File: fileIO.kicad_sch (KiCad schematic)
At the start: 24 parts, among them J3 USB_C, J5 Conn_02x03_Odd_Even, SW1 SW_Push

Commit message: Fix some checker complaints
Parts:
- TP1, TP19, TP2, TP20, TP26, TP27, TP29, TP30, TP31, TP32: value (none) -> SMD_TP; footprint (none) -> gkl_misc:TestPoint_Pad_D0.5mm
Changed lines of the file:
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@@
       (effects (font (size 1.27 1.27)) (justify right))
     )
-    (property "Value" "" (id 1) (at 43.3324 140.8938 0)
-      (effects (font (size 1.27 1.27)) (justify right) hide)
-    )
-    (property "Footprint" "" (id 2) (at 49.53 140.97 0)
+    (property "Value" "SMD_TP" (id 1) (at 43.3324 140.8938 0)
+      (effects (font (size 1.27 1.27)) (justify right) hide)
+    )
+    (property "Footprint" "gkl_misc:TestPoint_Pad_D0.5mm" (id 2) (at 49.53 140.97 0)
       (effects (font (size 1.27 1.27)) hide)
     )
@@
       (effects (font (size 1.27 1.27)) (justify right))
     )
-    (property "Value" "" (id 1) (at 43.3324 143.4338 0)
-      (effects (font (size 1.27 1.27)) (justify right) hide)
-    )
-    (property "Footprint" "" (id 2) (at 49.53 143.51 0)
+    (property "Value" "SMD_TP" (id 1) (at 43.3324 143.4338 0)
+      (effects (font (size 1.27 1.27)) (justify right) hide)
+    )
+    (property "Footprint" "gkl_misc:TestPoint_Pad_D0.5mm" (id 2) (at 49.53 143.51 0)
       (effects (font (size 1.27 1.27)) hide)
     )
@@
       (effects (font (size 1.27 1.27)) (justify right))
     )
-    (property "Value" "" (id 1) (at 43.3324 159.9438 0)
-      (effects (font (size 1.27 1.27)) (justify right) hide)
-    )
-    (property "Footprint" "" (id 2) (at 49.53 160.02 0)
+    (property "Value" "SMD_TP" (id 1) (at 43.3324 159.9438 0)
+      (effects (font (size 1.27 1.27)) (justify right) hide)
+    )
+    (property "Footprint" "gkl_misc:TestPoint_Pad_D0.5mm" (id 2) (at 49.53 160.02 0)
       (effects (font (size 1.27 1.27)) hide)
     )
@@
       (effects (font (size 1.27 1.27)) (justify right))
     )
-    (property "Value" "" (id 1) (at 43.3324 162.4838 0)
-      (effects (font (size 1.27 1.27)) (justify right) hide)
-    )
-    (property "Footprint" "" (id 2) (at 49.53 162.56 0)
+    (property "Value" "SMD_TP" (id 1) (at 43.3324 162.4838 0)
+      (effects (font (size 1.27 1.27)) (justify right) hide)
+    )
+    (property "Footprint" "gkl_misc:TestPoint_Pad_D0.5mm" (id 2) (at 49.53 162.56 0)
       (effects (font (size 1.27 1.27)) hide)
     )
@@
       (effects (font (size 1.27 1.27)) (justify right))
     )
-    (property "Value" "" (id 1) (at 43.3324 157.4038 0)
-      (effects (font (size 1.27 1.27)) (justify right) hide)
-    )
-    (property "Footprint" "" (id 2) (at 49.53 157.48 0)
+    (property "Value" "SMD_TP" (id 1) (at 43.3324 157.4038 0)
+      (effects (font (size 1.27 1.27)) (justify right) hide)
+    )
+    (property "Footprint" "gkl_misc:TestPoint_Pad_D0.5mm" (id 2) (at 49.53 157.48 0)
       (effects (font (size 1.27 1.27)) hide)
     )
@@
       (effects (font (size 1.27 1.27)) (justify right))
     )
-    (property "Value" "" (id 1) (at 43.3324 154.8638 0)
-      (effects (font (size 1.27 1.27)) (justify right) hide)
-    )
-    (property "Footprint" "" (id 2) (at 49.53 154.94 0)
+    (property "Value" "SMD_TP" (id 1) (at 43.3324 154.8638 0)
+      (effects (font (size 1.27 1.27)) (justify right) hide)
+    )
+    (property "Footprint" "gkl_misc:TestPoint_Pad_D0.5mm" (id 2) (at 49.53 154.94 0)
       (effects (font (size 1.27 1.27)) hide)
     )
@@
       (effects (font (size 1.27 1.27)) (justify right))
     )
-    (property "Value" "" (id 1) (at 40.4876 172.6438 0)
-      (effects (font (size 1.27 1.27)) (justify right) hide)
-    )
-    (property "Footprint" "" (id 2) (at 34.29 172.72 0)
+    (property "Value" "SMD_TP" (id 1) (at 40.4876 172.6438 0)
+      (effects (font (size 1.27 1.27)) (justify right) hide)
+    )
+    (property "Footprint" "gkl_misc:TestPoint_Pad_D0.5mm" (id 2) (at 34.29 172.72 0)
       (effects (font (size 1.27 1.27)) hide)
     )
@@
       (effects (font (size 1.27 1.27)) (justify right))
     )
-    (property "Value" "" (id 1) (at 40.4876 175.1838 0)
-      (effects (font (size 1.27 1.27)) (justify right) hide)
-    )
-    (property "Footprint" "" (id 2) (at 34.29 175.26 0)
+    (property "Value" "SMD_TP" (id 1) (at 40.4876 175.1838 0)
+      (effects (font (size 1.27 1.27)) (justify right) hide)
+    )
+    (property "Footprint" "gkl_misc:TestPoint_Pad_D0.5mm" (id 2) (at 34.29 175.26 0)
       (effects (font (size 1.27 1.27)) hide)
     )
@@
       (effects (font (size 1.27 1.27)) (justify right))
     )
-    (property "Value" "" (id 1) (at 72.5424 140.8938 0)
-      (effects (font (size 1.27 1.27)) (justify right) hide)
-    )
-    (property "Footprint" "" (id 2) (at 78.74 140.97 0)
+    (property "Value" "SMD_TP" (id 1) (at 72.5424 140.8938 0)
+      (effects (font (size 1.27 1.27)) (justify right) hide)
+    )
+    (property "Footprint" "gkl_misc:TestPoint_Pad_D0.5mm" (id 2) (at 78.74 140.97 0)
       (effects (font (size 1.27 1.27)) hide)
     )
@@
       (effects (font (size 1.27 1.27)) (justify right))
     )
-    (property "Value" "" (id 1) (at 72.5424 143.4338 0)
-      (effects (font (size 1.27 1.27)) (justify right) hide)
-    )
-    (property "Footprint" "" (id 2) (at 78.74 143.51 0)
-      (effects (font (size 1.27 1.27)) hide)
-    )
+    (property "Value" "SMD_TP" (id 1) (at 72.5424 143.4338 0)
+      (effects (font (size 1.27 1.27)) (justify right) hide)
+    )
+    (property "Footprint" "gkl_misc:TestPoint_Pad_D0.5mm" (id 2) (at 78.74 143.51 0)
+      (effects (font (size 1.27 1.27)) hide)
+    )

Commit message: Update Mouser prices
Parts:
- C76: Pricing (EUR) 0,11 -> 0,09
- D1: Pricing (EUR) 1,85 -> 2,03
- J3: Pricing (EUR) 0,71 -> 0,77
- R21, R29, R4: Pricing (EUR) 0,11 -> 0,10
- R22, R23, R24, R32, R33: Pricing (EUR) 0,09 -> 0,10
- SW1: Pricing (EUR) 4,02 -> 5,11
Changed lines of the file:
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@@
       (effects (font (size 1.27 1.27)) hide)
     )
-    (property "Pricing (EUR)" "0,71" (id 7) (at 38.1 77.47 0)
+    (property "Pricing (EUR)" "0,77" (id 7) (at 38.1 77.47 0)
       (effects (font (size 1.27 1.27)) hide)
     )
@@
       (effects (font (size 1.27 1.27)) hide)
     )
-    (property "Pricing (EUR)" "0,09" (id 7) (at 214.63 29.21 0)
+    (property "Pricing (EUR)" "0,10" (id 7) (at 214.63 29.21 0)
       (effects (font (size 1.27 1.27)) hide)
     )
@@
       (effects (font (size 1.27 1.27)) hide)
     )
-    (property "Pricing (EUR)" "0,09" (id 7) (at 214.63 34.29 0)
+    (property "Pricing (EUR)" "0,10" (id 7) (at 214.63 34.29 0)
       (effects (font (size 1.27 1.27)) hide)
     )
@@
       (effects (font (size 1.27 1.27)) hide)
     )
-    (property "Pricing (EUR)" "4,02" (id 7) (at 133.35 44.45 0)
+    (property "Pricing (EUR)" "5,11" (id 7) (at 133.35 44.45 0)
       (effects (font (size 1.27 1.27)) hide)
     )
@@
       (effects (font (size 1.27 1.27)) hide)
     )
-    (property "Pricing (EUR)" "0,11" (id 7) (at 144.78 38.1 0)
+    (property "Pricing (EUR)" "0,10" (id 7) (at 144.78 38.1 0)
       (effects (font (size 1.27 1.27)) hide)
     )
@@
       (effects (font (size 1.27 1.27)) hide)
     )
-    (property "Pricing (EUR)" "0,11" (id 7) (at 148.59 49.53 0)
+    (property "Pricing (EUR)" "0,09" (id 7) (at 148.59 49.53 0)
       (effects (font (size 1.27 1.27)) hide)
     )
@@
       (effects (font (size 1.27 1.27)) hide)
     )
-    (property "Pricing (EUR)" "0,11" (id 7) (at 76.2 80.01 0)
+    (property "Pricing (EUR)" "0,10" (id 7) (at 76.2 80.01 0)
       (effects (font (size 1.27 1.27)) hide)
     )
@@
       (effects (font (size 1.27 1.27)) hide)
     )
-    (property "Pricing (EUR)" "0,11" (id 7) (at 76.2 77.47 0)
+    (property "Pricing (EUR)" "0,10" (id 7) (at 76.2 77.47 0)
       (effects (font (size 1.27 1.27)) hide)
     )
@@
       (effects (font (size 1.27 1.27)) hide)
     )
-    (property "Pricing (EUR)" "0,09" (id 7) (at 214.63 39.37 0)
+    (property "Pricing (EUR)" "0,10" (id 7) (at 214.63 39.37 0)
       (effects (font (size 1.27 1.27)) hide)
     )
@@
       (effects (font (size 1.27 1.27)) hide)
     )
-    (property "Pricing (EUR)" "1,85" (id 7) (at 226.06 34.29 0)
+    (property "Pricing (EUR)" "2,03" (id 7) (at 226.06 34.29 0)
       (effects (font (size 1.27 1.27)) hide)
     )
@@
       (effects (font (size 1.27 1.27)) hide)
     )
-    (property "Pricing (EUR)" "0,09" (id 7) (at 59.69 67.31 0)
+    (property "Pricing (EUR)" "0,10" (id 7) (at 59.69 67.31 0)
       (effects (font (size 1.27 1.27)) hide)
     )
@@
       (effects (font (size 1.27 1.27)) hide)
     )
-    (property "Pricing (EUR)" "0,09" (id 7) (at 59.69 69.85 0)
-      (effects (font (size 1.27 1.27)) hide)
-    )
+    (property "Pricing (EUR)" "0,10" (id 7) (at 59.69 69.85 0)
+      (effects (font (size 1.27 1.27)) hide)
+    )

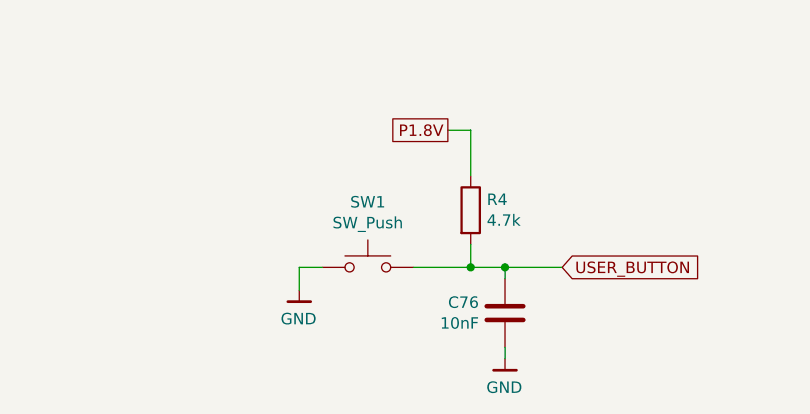
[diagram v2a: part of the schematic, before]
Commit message: Replace HyperRAM with 3V Winbond part
Also remove PSC/PSC# as they are not used on 3V parts.
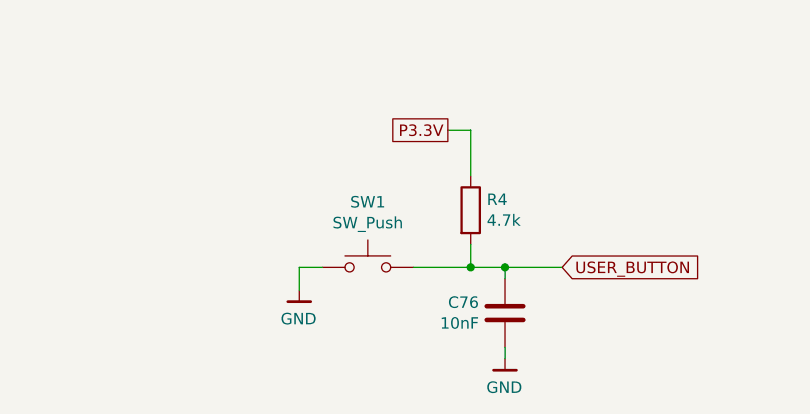
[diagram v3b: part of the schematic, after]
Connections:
- net P1.8V: no longer R4.1
- net P3.3V: now also R4.1
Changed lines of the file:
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@@
-    )
-  )
-  (global_label "P1.8V" (shape passive) (at 142.24 29.21 180) (fields_autoplaced)
-    (effects (font (size 1.27 1.27)) (justify right))
-    (property "Intersheet References" "${INTERSHEET_REFS}" (id 0) (at 0 0 0)
-      (effects (font (size 1.27 1.27)) hide)
     )
   )
@@
       (effects (font (size 1.27 1.27)) hide)
     )
+  )
+  (global_label "P3.3V" (shape passive) (at 142.24 29.21 180) (fields_autoplaced)
+    (effects (font (size 1.27 1.27)) (justify right))
+    (property "Intersheet References" "${INTERSHEET_REFS}" (id 0) (at -104.14 -35.56 0)
+      (effects (font (size 1.27 1.27)) hide)
+    )

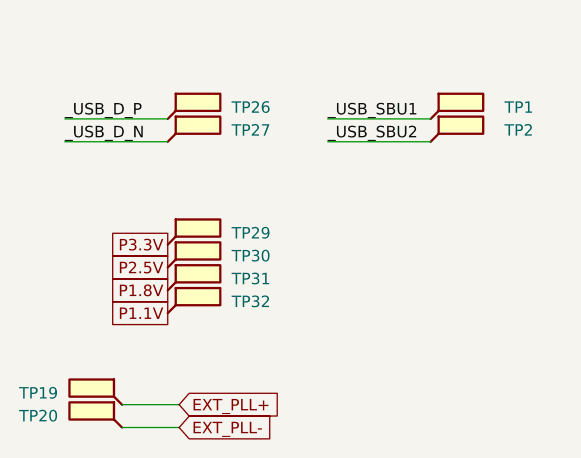
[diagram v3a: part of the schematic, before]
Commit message: Remove 1.8V power supply
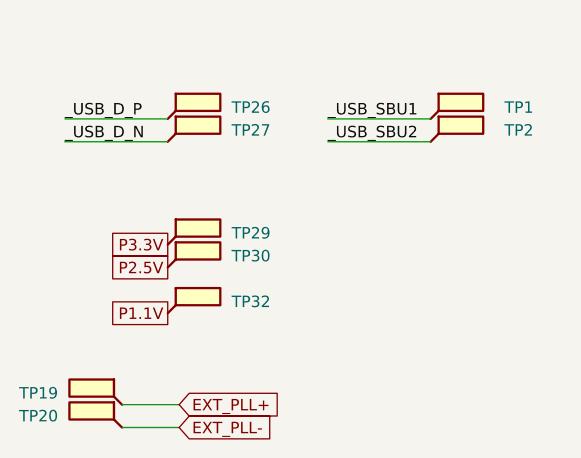
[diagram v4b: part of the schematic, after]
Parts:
- removed TP31: SMD_TP, gkl_misc:TestPoint_Pad_D0.5mm, symbol Connector:TestPoint_Flag
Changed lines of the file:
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@@
-    )
-  )
-  (global_label "P1.8V" (shape passive) (at 44.45 160.02 180) (fields_autoplaced)
-    (effects (font (size 1.27 1.27)) (justify right))
-    (property "Intersheet References" "${INTERSHEET_REFS}" (id 0) (at 0 0 0)
-      (effects (font (size 1.27 1.27)) hide)
     )
   )
@@
       (effects (font (size 1.27 1.27)) hide)
     )
-    (pin "1")
-  )
-  (symbol (lib_id "Connector:TestPoint_Flag") (at 44.45 160.02 0) (unit 1)
-    (in_bom no) (on_board yes)
-    (property "Reference" "TP31" (id 0) (at 55.88 158.75 0)
-      (effects (font (size 1.27 1.27)) (justify right))
-    )
-    (property "Value" "SMD_TP" (id 1) (at 43.3324 159.9438 0)
-      (effects (font (size 1.27 1.27)) (justify right) hide)
-    )
-    (property "Footprint" "gkl_misc:TestPoint_Pad_D0.5mm" (id 2) (at 49.53 160.02 0)
-      (effects (font (size 1.27 1.27)) hide)
-    )
-    (property "Datasheet" "~" (id 3) (at 49.53 160.02 0)
-      (effects (font (size 1.27 1.27)) hide)
-    )

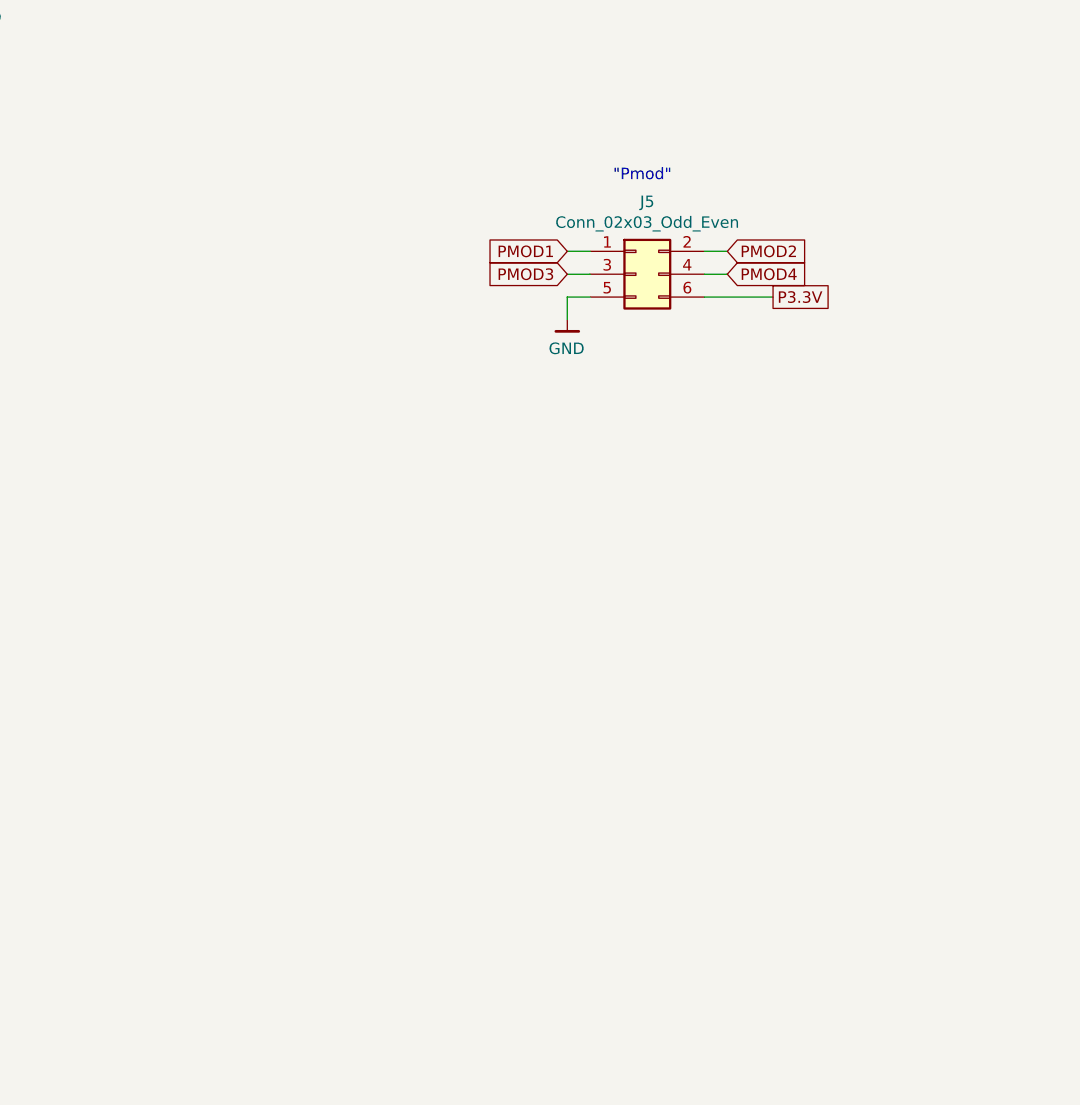
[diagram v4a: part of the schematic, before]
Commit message: Add a dual PMOD connector with official shape
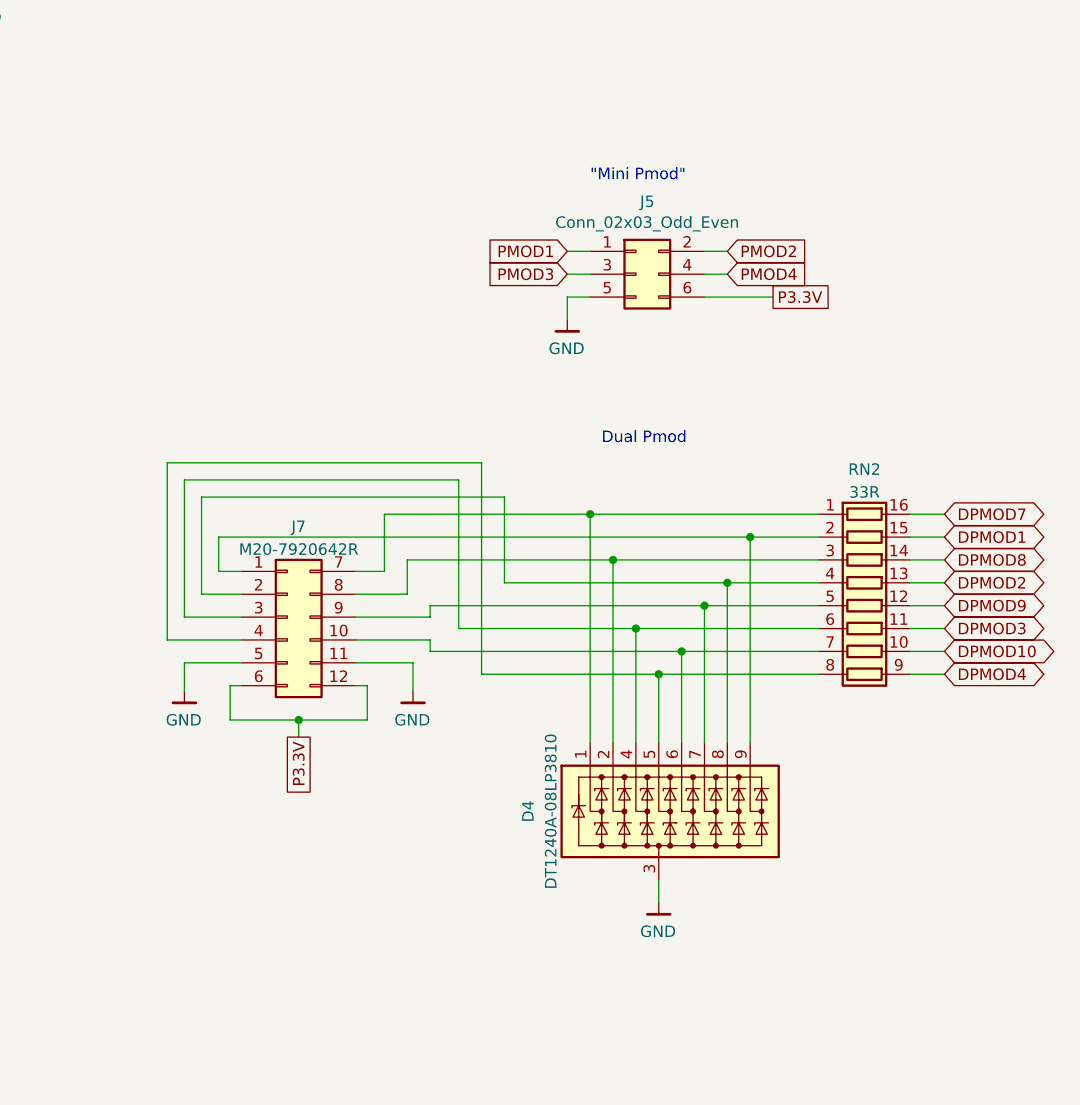
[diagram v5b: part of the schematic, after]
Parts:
- added D4: DT1240A-08LP3810, Package_DFN_QFN:UDFN-9_1.0x3.8mm_P0.5mm, symbol Power_Protection:DT1240A-08LP3810
- added J7: M20-7920642R, Harwin:M207920642R, symbol Connector_Generic:Conn_02x06_Top_Bottom
- added RN2: 33R, Resistor_SMD:R_Array_Convex_8x0602, symbol Device:R_Pack08
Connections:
- net GND: now also D4.3 (A), J7.11 (Pin_11), J7.5 (Pin_5)
- net P3.3V: now also J7.12 (Pin_12), J7.6 (Pin_6)
- new net: D4.1 (K1), J7.7 (Pin_7), RN2.1 (R1.1)
- new net: D4.2 (K2), J7.8 (Pin_8), RN2.3 (R3.1)
- new net: D4.4 (K3), J7.3 (Pin_3), RN2.6 (R6.1)
- new net: D4.5 (K4), J7.4 (Pin_4), RN2.8 (R8.1)
- new net: D4.6 (K5), J7.10 (Pin_10), RN2.7 (R7.1)
- new net: D4.7 (K6), J7.9 (Pin_9), RN2.5 (R5.1)
- new net: D4.8 (K7), J7.2 (Pin_2), RN2.4 (R4.1)
- new net: D4.9 (K8), J7.1 (Pin_1), RN2.2 (R2.1)
- new net DPMOD1: RN2.15 (R2.2)
- new net DPMOD10: RN2.10 (R7.2)
- new net DPMOD2: RN2.13 (R4.2)
- new net DPMOD3: RN2.11 (R6.2)
- new net DPMOD4: RN2.9 (R8.2)
- new net DPMOD7: RN2.16 (R1.2)
- new net DPMOD8: RN2.14 (R3.2)
- new net DPMOD9: RN2.12 (R5.2)
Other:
- note added: ""Mini Pmod""
- note added: "Dual Pmod"
- note removed: ""Pmod""
